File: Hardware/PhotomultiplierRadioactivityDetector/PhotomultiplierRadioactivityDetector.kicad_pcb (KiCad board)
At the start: 2 copper layers, 100 x 100 mm, 135 parts, among them J13 Conn_01x02_Female, J14 Conn_01x04, J15 Conn_02x05_Counter_Clockwise, Q1 2N7002, Q2 Q_NPN_BEC, Q3 Q_NMOS_GDS, Q4 Q_NJFET_DGS, Q5 Q_NJFET_DGS, Q6 Q_NJFET_DGS, U1 TL074, U2 TL074, U3 MCP3425A0T-ECH, U4 LM3488, U5 STM8S003F3P, U6 TL074, U7 TL074

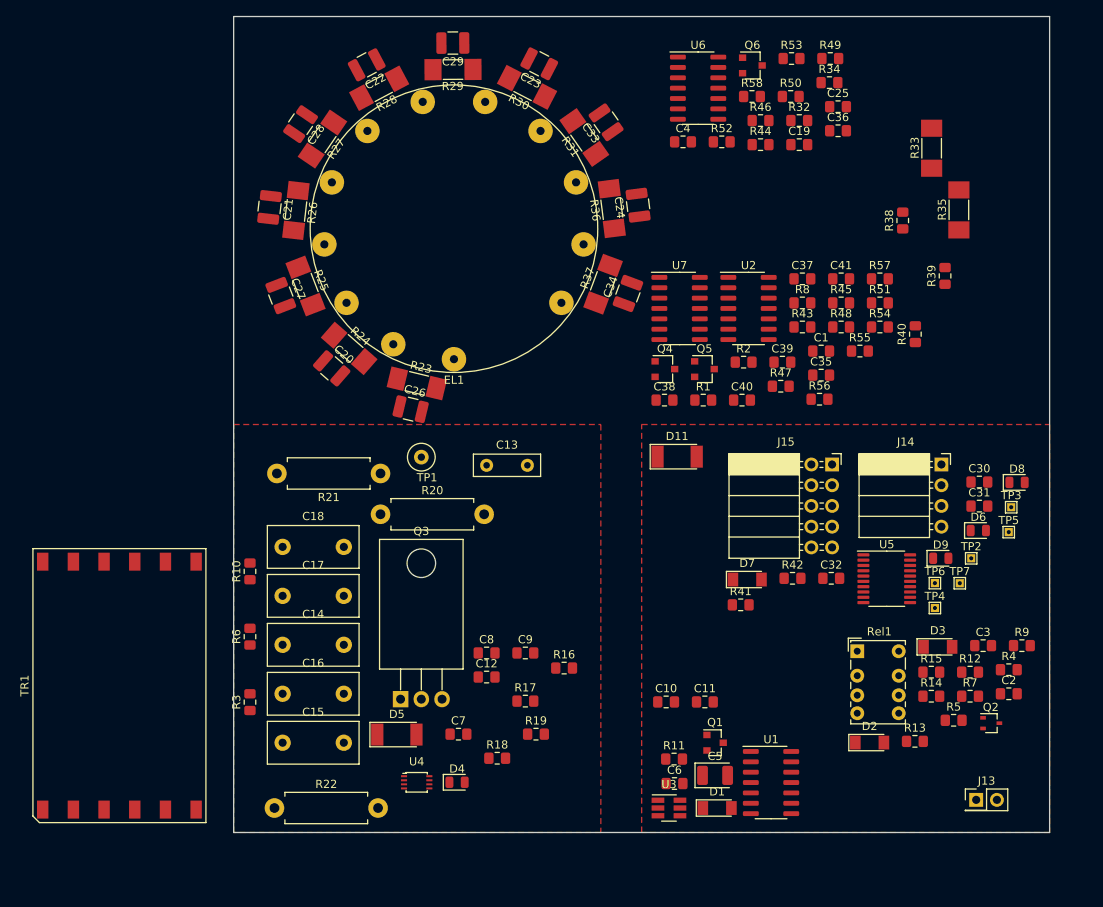
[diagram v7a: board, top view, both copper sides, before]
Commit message: draft of modules placement
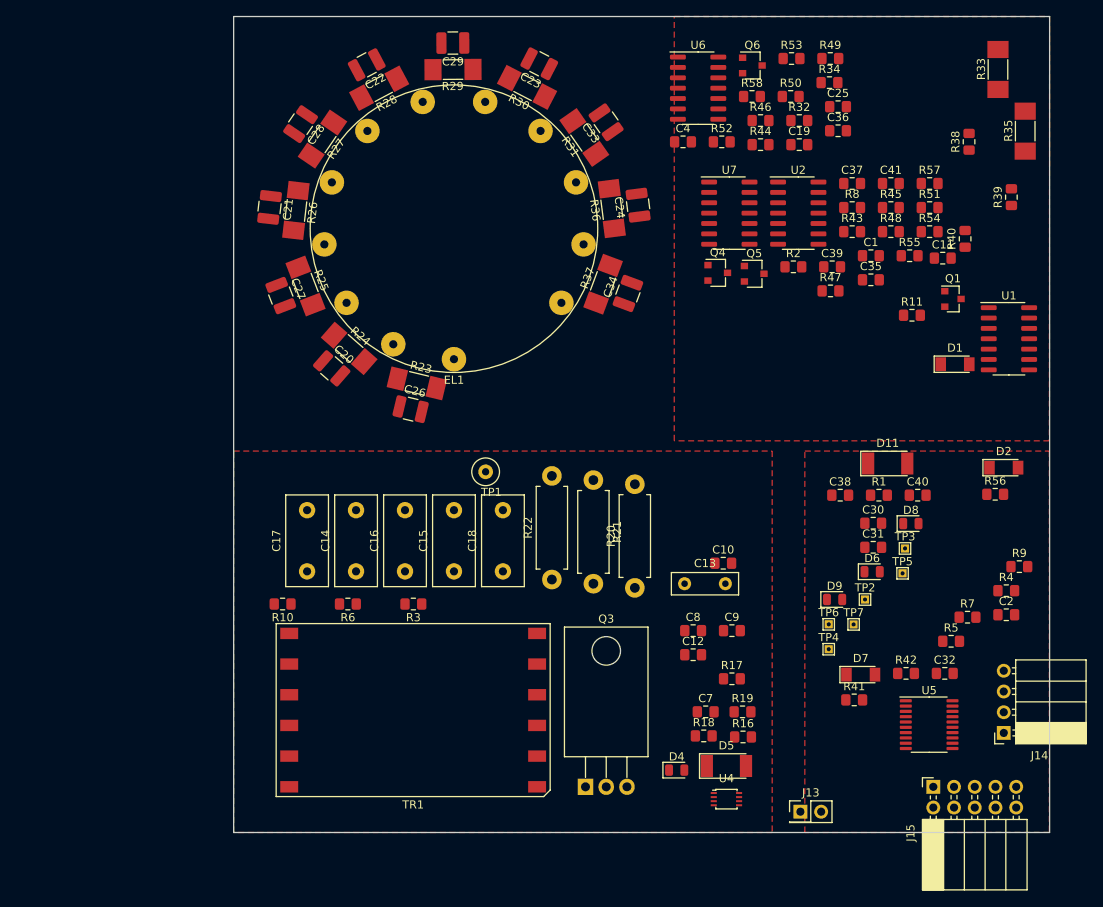
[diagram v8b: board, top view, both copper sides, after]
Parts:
- removed C3: 10n, Capacitor_SMD:C_0805_2012Metric_Pad1.15x1.40mm_HandSolder
- removed C5: 10u, Capacitor_Tantalum_SMD:CP_EIA-3528-21_Kemet-B
- removed C6: 100n, Capacitor_SMD:C_0805_2012Metric_Pad1.15x1.40mm_HandSolder
- removed D3: 1n148, Diode_SMD:D_MiniMELF
- removed Q2: Q_NPN_BEC, Package_TO_SOT_SMD:SOT-323_SC-70
- removed R12: 1k, Resistor_SMD:R_0805_2012Metric_Pad1.15x1.40mm_HandSolder
- removed R13: 10k, Resistor_SMD:R_0805_2012Metric_Pad1.15x1.40mm_HandSolder
- removed R14, R15: 0R, Resistor_SMD:R_0805_2012Metric_Pad1.15x1.40mm_HandSolder
- removed Rel1: RSM850B-6112-85-1005, Relay_THT:Relay_DPDT_Omron_G6K-2P-Y
- removed U3: MCP3425A0T-ECH, Package_TO_SOT_SMD:SOT-23-6_Handsoldering
- moved C11 61.7 mm to (111.9, 119.6)
- moved D1 61.7 mm to (113.4, 132.6)
- moved Q1 61.7 mm to (113.2, 124.6)
- moved R11 61.7 mm to (108.1, 126.6)
- moved U1 61.7 mm to (120.0, 129.5)
- moved R22 44.0 mm to (64.0, 159.0), turned to 90 degrees
- moved J15 41.4 mm to (110.7, 184.4), turned to 90 degrees
- moved D5 40.6 mm to (85.4, 181.8)
- moved U4 38.0 mm to (85.4, 185.9)
- moved D2 37.5 mm to (119.4, 145.3)
- moved TR1 36.1 mm to (47.0, 175.0), turned to 90 degrees
- moved J14 33.8 mm to (119.4, 177.8), turned to 180 degrees
- moved R20 32.4 mm to (74.2, 160.0), turned to 90 degrees
- moved C7 30.4 mm to (82.9, 175.2)
- moved C15 29.7 mm to (52.0, 158.0), turned to 90 degrees
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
